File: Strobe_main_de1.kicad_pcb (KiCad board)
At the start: 4 copper layers, 100 x 100 mm, 167 parts, among them J1001 Header, J302 T44007, J303 T44007, J304 10146581-060_M, J305 T44007, J306 T44007, J701 ZHOURI DC3, J800 Molex 430451227, J901 Header, Q100 MDT7N65, Q301 MPF3N150, Q303 IXYH55N120, Q304 IXYH55N120, Q305 IXYH55N120, U100 LM217MDT, U101 AMS1117-3.3, U102 AMS1117-3.3, U301 IRS2184, U401 TSV912IDT, U501 STM32G431K8Tx, U601 ISO1541, U602 ISO6741, Y501 20 MHz

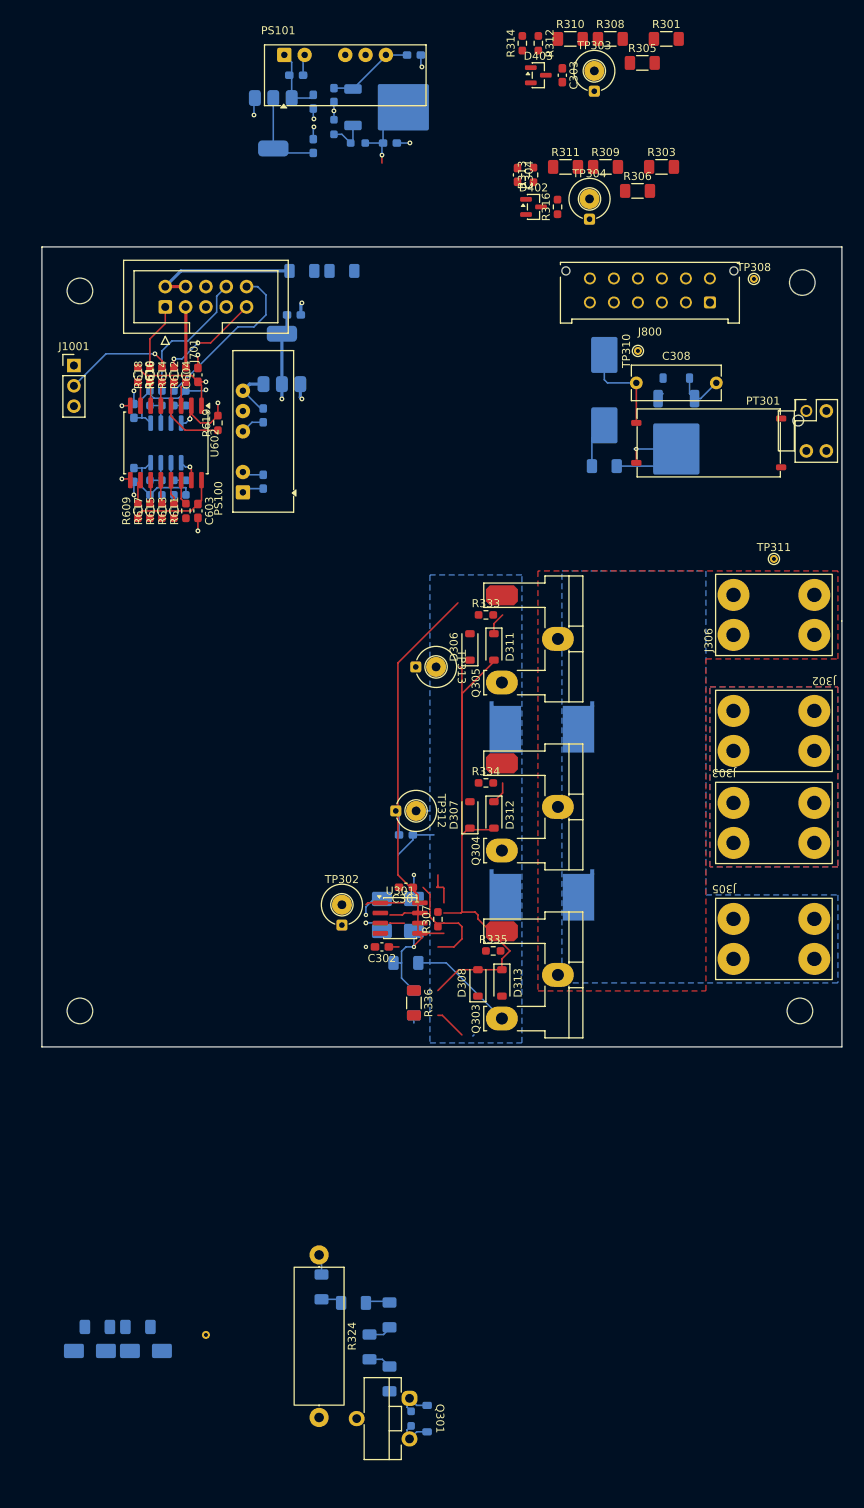
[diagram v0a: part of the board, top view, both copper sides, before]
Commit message: New placement strategy
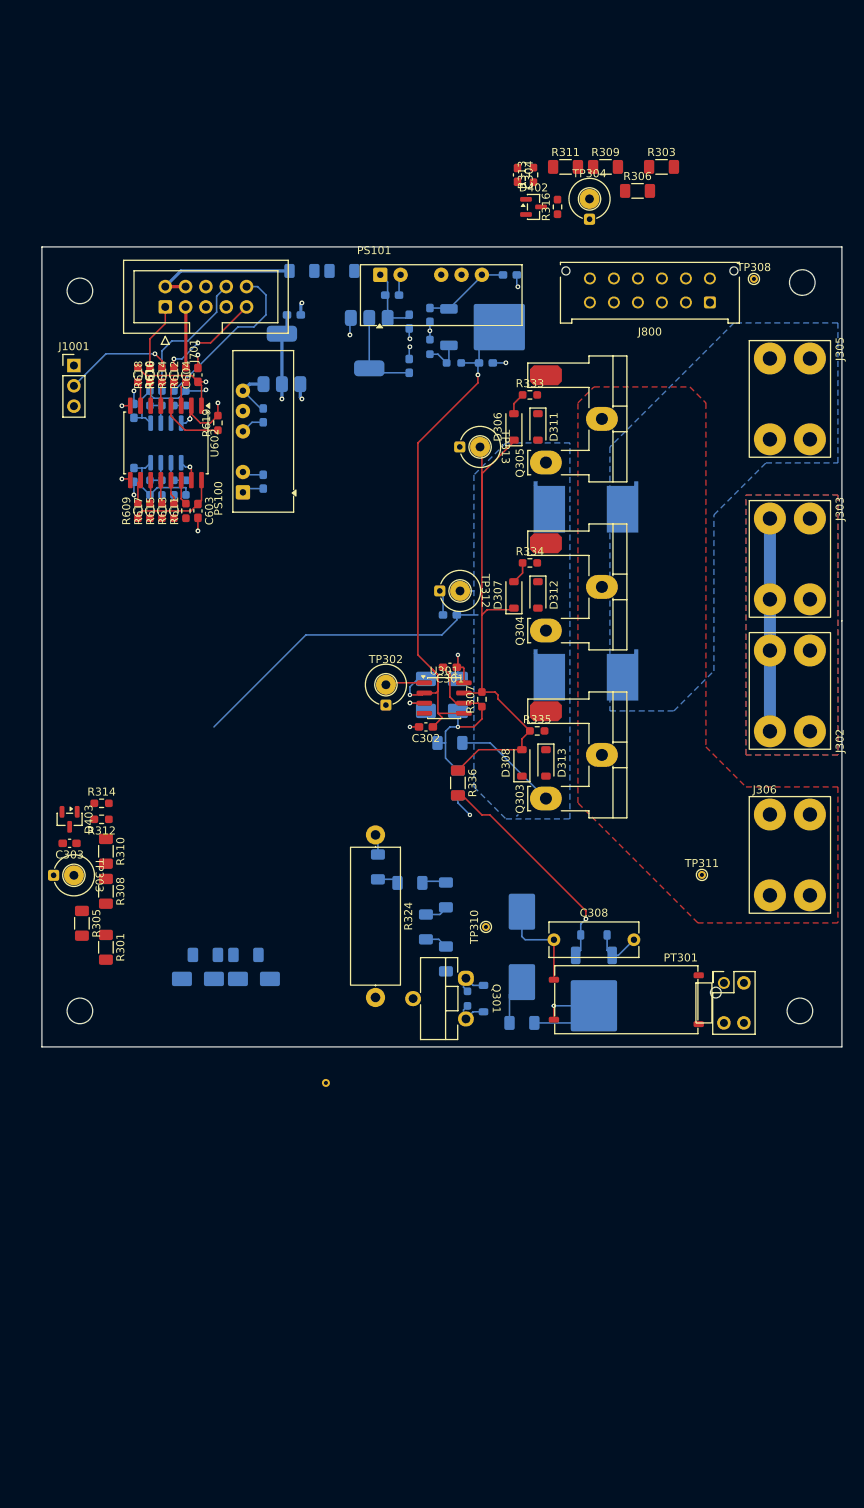
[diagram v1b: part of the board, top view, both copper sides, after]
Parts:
- moved R301 133.4 mm to (168.0, 137.6), turned to -90 degrees
- moved R305 128.4 mm to (165.0, 134.6), turned to -90 degrees
- moved R308 123.8 mm to (168.0, 130.6), turned to -90 degrees
- moved TP303 119.4 mm to (162.7, 128.6), turned to -90 degrees
- moved R310 117.0 mm to (168.0, 125.5), turned to -90 degrees
- moved C303 114.1 mm to (163.5, 124.5), turned to 180 degrees
- moved R312 111.3 mm to (167.5, 121.5), turned to 180 degrees
- moved D403 109.9 mm to (163.5, 121.5), turned to -90 degrees
- moved R314 108.6 mm to (167.5, 119.5), turned to 0 degrees
- moved TP310 74.5 mm to (215.5, 135.0)
- moved J304 72.2 mm to (246.5, 144.5)
- moved C308 70.4 mm to (224.0, 136.6)
- moved D304 70.4 mm to (220.0, 137.5)
- moved D310 70.4 mm to (229.0, 136.0)
- moved Q100 70.4 mm to (229.0, 143.6)
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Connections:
- J800 pad 10: /Block Diagram/Vbus_ctrl -> unconnected-(J800-Pin_10-Pad10)
- J800 pad 12: unconnected-(J800-Pin_12-Pad12) -> /Block Diagram/Vbus_ctrl
- J800 pad 4: /Block Diagram/SH0 -> unconnected-(J800-Pin_4-Pad4)
- J800 pad 5: /Block Diagram/MCU/SUP_TX -> /Block Diagram/SH0
- J800 pad 9: /Block Diagram/SH5 -> unconnected-(J800-Pin_9-Pad9)
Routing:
- net /Block Diagram/S1k: track 60.3 -> 115.0 mm
- net /Block Diagram/Lamp driver/Mon_IL: track 21.2 -> 54.4 mm
- net /Block Diagram/SH0: track 45.0 -> 69.1 mm, vias 12 -> 13
- net /Block Diagram/Lamp driver/G_TP_DRV: track 4.91 -> 28.1 mm, vias 0 -> 1
- net /Block Diagram/Lamp driver/DRV_OUT: track 68.8 -> 74.4 mm
- net /Block Diagram/Lamp driver/G_L_D_2: track 2.80 -> 0.00 mm
- net /Block Diagram/Lamp driver/G_L_D1: track 2.80 -> 0.00 mm
- net /Block Diagram/SH20: track 72.7 -> 71.6 mm
- added copper zone on In1.Cu, net /Block Diagram/Lamp driver/LMP
